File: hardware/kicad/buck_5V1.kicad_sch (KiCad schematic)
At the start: 17 parts, among them J1 V12_IN, J2 V5_OUT, U1 LMZ23610TZ/NOPB

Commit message: feat: added pcb for buck 5V1
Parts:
- added D1: LED, LED_THT:LED_D3.0mm, symbol Device:LED
- added NT1: NetTie_2, NetTie:NetTie-2_SMD_Pad2.0mm, symbol Device:NetTie_2
- added R6: 1k, Resistor_THT:R_Axial_DIN0207_L6.3mm_D2.5mm_P10.16mm_Horizontal, symbol Device:R
- added TP1: V12_IN, TestPoint:TestPoint_Pad_D2.5mm, symbol Connector:TestPoint
- added TP2: GND, TestPoint:TestPoint_Pad_D2.5mm, symbol Connector:TestPoint
- added TP3: V5, TestPoint:TestPoint_Pad_D2.5mm, symbol Connector:TestPoint
- C1, C2, C3, C4, C5, C8, C9: footprint (none) -> Capacitor_THT:C_Disc_D7.0mm_W2.5mm_P5.00mm
- C6, C7: footprint (none) -> Capacitor_Tantalum_SMD:CP_EIA-7343-43_Kemet-X
- J1, J2: footprint (none) -> Terminals:CUI_TB002-500-02BE
- R1, R2, R3, R4, R5: footprint (none) -> Resistor_THT:R_Axial_DIN0207_L6.3mm_D2.5mm_P10.16mm_Horizontal
- U1: footprint NDY0011A_N -> buck_5V:NDY0011A_L
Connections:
- net V12_IN: now reaches C1.1, C2.1, C3.1, C8.1, J1.1 (Pin_1), R1.1, U1.1 (VIN), U1.2 (VIN)
- net V12_IN: now also TP1.1
- net AGND: now reaches C1.2, C2.2, C3.2, C8.2, J1.2 (Pin_2), R2.1, U1.3 (SYNC), U1.5 (AGND), U1.6 (AGND)
- net AGND: now also NT1.1, TP2.1; no longer C4.2, C6.2, C7.2, C9.2, J2.2 (Pin_2), R5.1, U1.12 (EP)
- net V5_OUT: now reaches C5.1, C6.1, C7.1, C9.1, J2.1 (Pin_1), R4.2, U1.10 (VOUT), U1.11 (VOUT)
- net V5_OUT: now also R6.2, TP3.1
- new net: D1.2 (A), R6.1
- new net PGND: C4.2, C6.2, C7.2, C9.2, D1.1 (K), J2.2 (Pin_2), NT1.2, R5.1, U1.12 (EP)
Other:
- moved on the sheet: J2

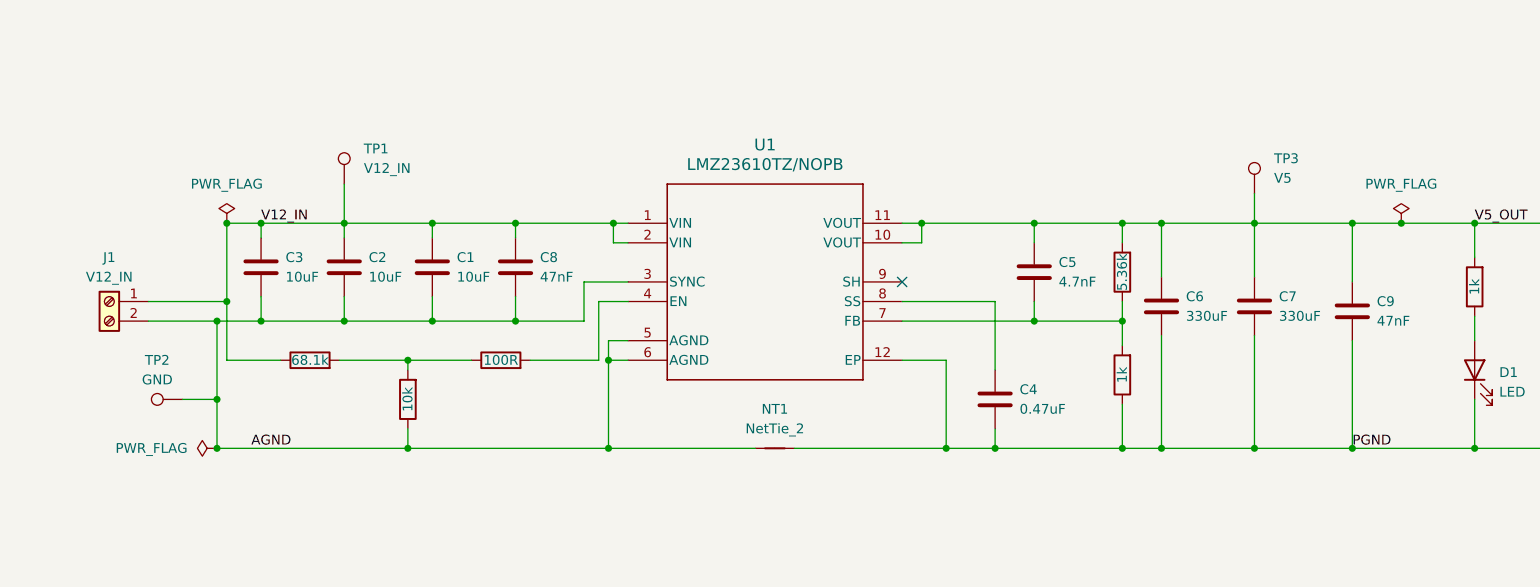
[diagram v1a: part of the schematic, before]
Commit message: fix: package change & pcb comp placement - buck5V1
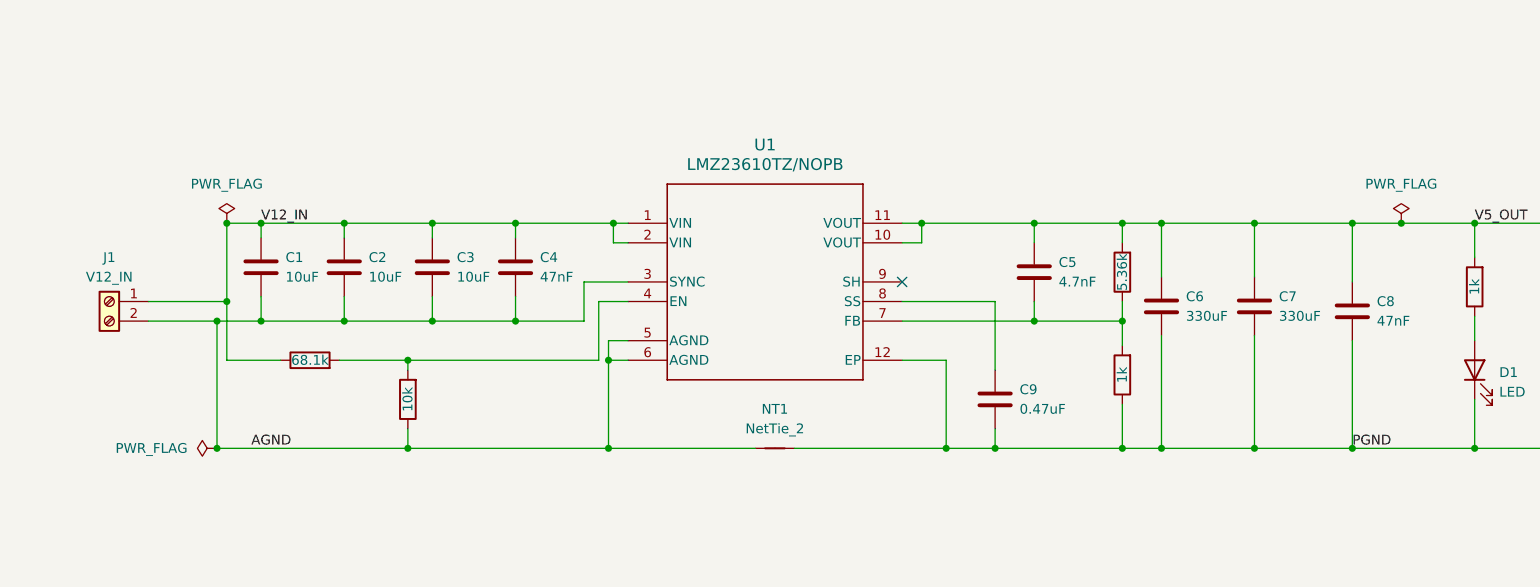
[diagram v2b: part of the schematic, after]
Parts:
- removed R3: 100R, Resistor_THT:R_Axial_DIN0207_L6.3mm_D2.5mm_P10.16mm_Horizontal, symbol Device:R
- removed TP1: V12_IN, TestPoint:TestPoint_Pad_D2.5mm, symbol Connector:TestPoint
- removed TP2: GND, TestPoint:TestPoint_Pad_D2.5mm, symbol Connector:TestPoint
- removed TP3: V5, TestPoint:TestPoint_Pad_D2.5mm, symbol Connector:TestPoint
- C1: renamed from C3; footprint Capacitor_THT:C_Disc_D7.0mm_W2.5mm_P5.00mm -> Capacitor_SMD:C_0805_2012Metric_Pad1.18x1.45mm_HandSolder
- C2, C5: footprint Capacitor_THT:C_Disc_D7.0mm_W2.5mm_P5.00mm -> Capacitor_SMD:C_0805_2012Metric_Pad1.18x1.45mm_HandSolder
- C3: renamed from C1; footprint Capacitor_THT:C_Disc_D7.0mm_W2.5mm_P5.00mm -> Capacitor_SMD:C_0805_2012Metric_Pad1.18x1.45mm_HandSolder
- C4: renamed from C8; footprint Capacitor_THT:C_Disc_D7.0mm_W2.5mm_P5.00mm -> Capacitor_SMD:C_0805_2012Metric_Pad1.18x1.45mm_HandSolder
- C6, C7: footprint Capacitor_Tantalum_SMD:CP_EIA-7343-43_Kemet-X -> Capacitor_THT:C_Radial_D6.3mm_H5.0mm_P2.50mm
- C8: renamed from C9; footprint Capacitor_THT:C_Disc_D7.0mm_W2.5mm_P5.00mm -> Capacitor_SMD:C_0805_2012Metric_Pad1.18x1.45mm_HandSolder
- C9: renamed from C4; footprint Capacitor_THT:C_Disc_D7.0mm_W2.5mm_P5.00mm -> Capacitor_SMD:C_0805_2012Metric_Pad1.18x1.45mm_HandSolder
- R1: renamed from R4; footprint Resistor_THT:R_Axial_DIN0207_L6.3mm_D2.5mm_P10.16mm_Horizontal -> Resistor_SMD:R_0805_2012Metric_Pad1.20x1.40mm_HandSolder
- R2: renamed from R6; footprint Resistor_THT:R_Axial_DIN0207_L6.3mm_D2.5mm_P10.16mm_Horizontal -> Resistor_SMD:R_0805_2012Metric_Pad1.20x1.40mm_HandSolder
- R3: renamed from R1; footprint Resistor_THT:R_Axial_DIN0207_L6.3mm_D2.5mm_P10.16mm_Horizontal -> Resistor_SMD:R_0805_2012Metric_Pad1.20x1.40mm_HandSolder
- R4: renamed from R5; footprint Resistor_THT:R_Axial_DIN0207_L6.3mm_D2.5mm_P10.16mm_Horizontal -> Resistor_SMD:R_0805_2012Metric_Pad1.20x1.40mm_HandSolder
- R5: renamed from R2; footprint Resistor_THT:R_Axial_DIN0207_L6.3mm_D2.5mm_P10.16mm_Horizontal -> Resistor_SMD:R_0805_2012Metric_Pad1.20x1.40mm_HandSolder
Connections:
- net at U1.4 (EN): now also R3.2, R5.2
